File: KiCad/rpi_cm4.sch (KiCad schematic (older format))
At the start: 8 parts

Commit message: Update schematic
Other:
- note added: "check pull ups/downs on RPi power control pins"
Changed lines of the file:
@@
 $Descr A4 11693 8268
 encoding utf-8
-Sheet 3 5
+Sheet 2 5
 Title "RPi Compute Module 4 Section"
 Date "2020-12-03"
@@
 	1    0    0    -1
 $EndComp
+Text Notes 800  6250 0    50   ~ 0
+check pull ups/downs on RPi power control pins
 $EndSCHEMATC

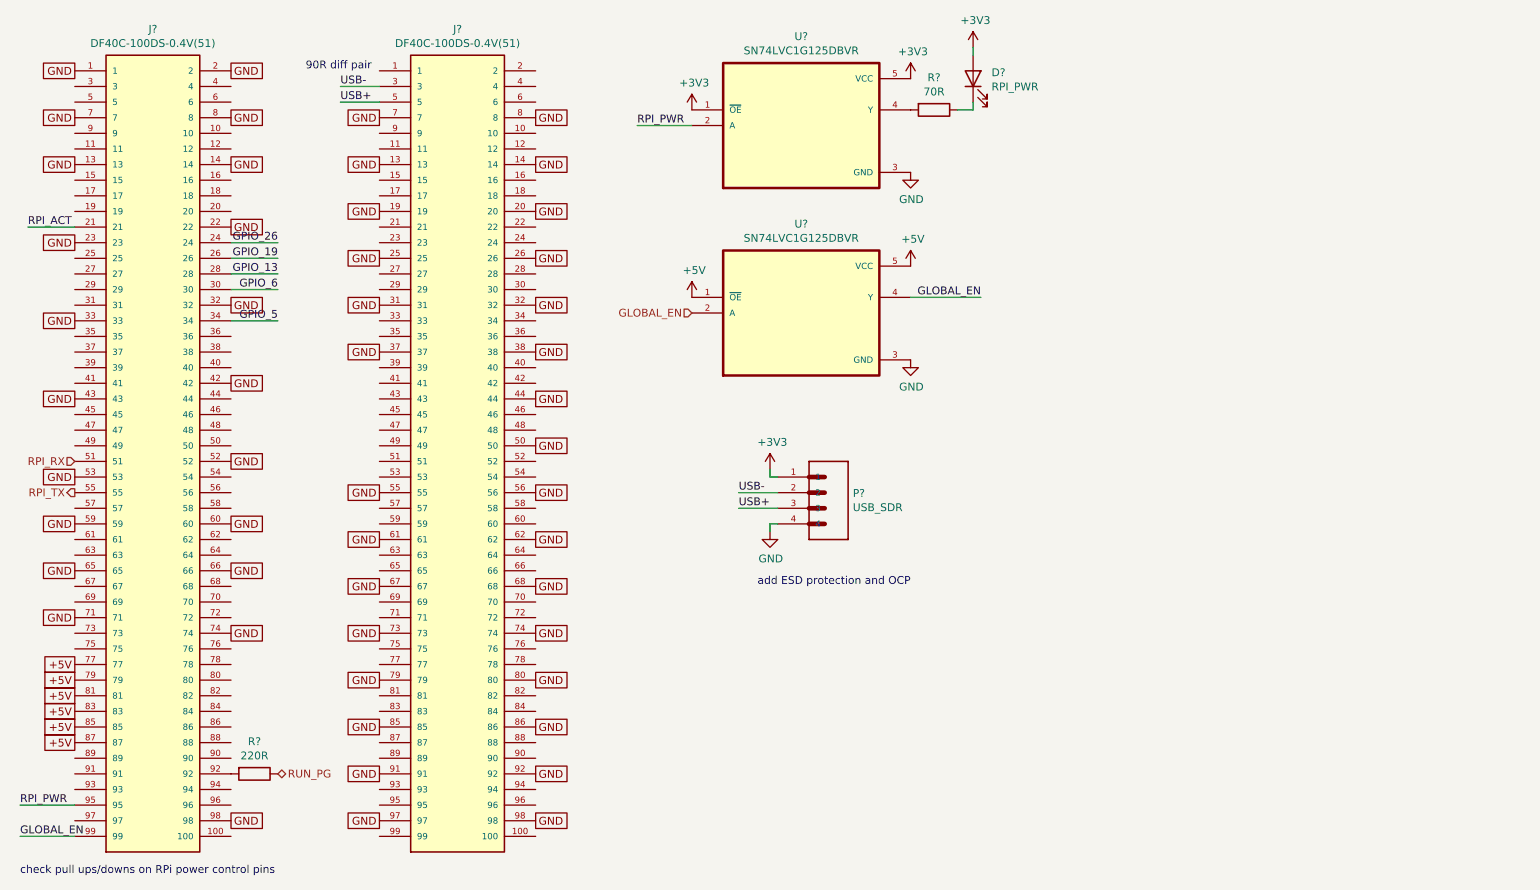
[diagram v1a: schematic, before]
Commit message: Finalized schematic and created S/F associations
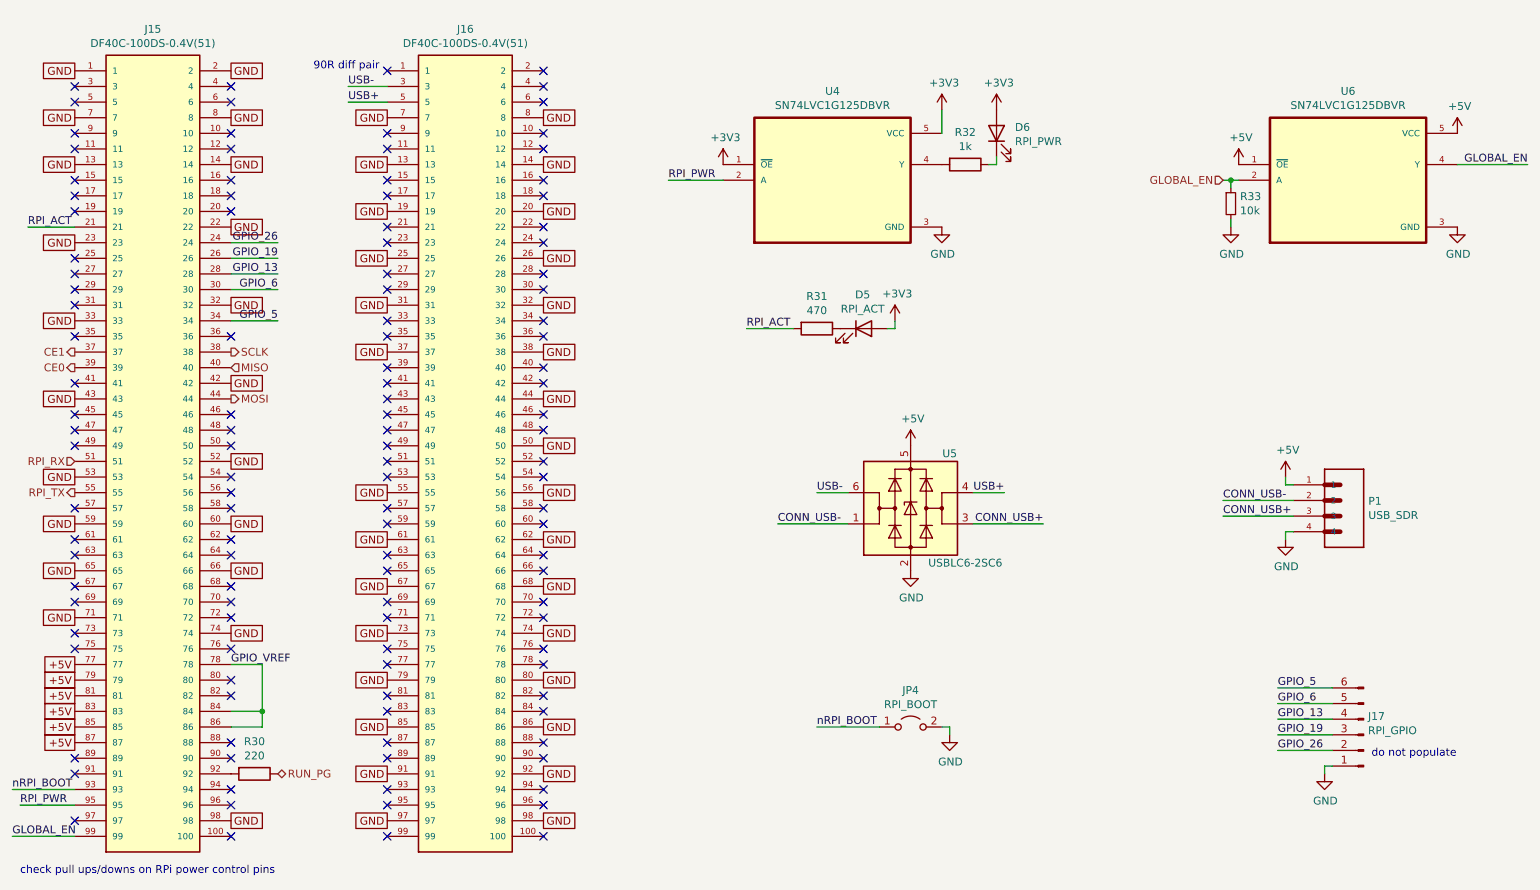
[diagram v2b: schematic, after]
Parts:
- added D5: RPI_ACT, LED_SMD:LED_0603_1608Metric_Pad1.05x0.95mm_HandSolder, symbol Device:LED
- added J17: RPI_GPIO, Connector_PinHeader_1.00mm:PinHeader_1x06_P1.00mm_Vertical, symbol Connector:Conn_01x06_Male
- added JP4: RPI_BOOT, TestPoint:TestPoint_2Pads_Pitch2.54mm_Drill0.8mm, symbol Jumper:Jumper_2_Open
- added R31: 470, Resistor_SMD:R_0603_1608Metric_Pad1.05x0.95mm_HandSolder, symbol Device:R
- added R33: 10k, Resistor_SMD:R_0603_1608Metric_Pad1.05x0.95mm_HandSolder, symbol Device:R_Small
- added U5: USBLC6-2SC6, Package_TO_SOT_SMD:SOT-23-6, symbol Power_Protection:USBLC6-2SC6
- D6: renamed from D?; footprint (none) -> LED_SMD:LED_0603_1608Metric_Pad1.05x0.95mm_HandSolder
- J15, J16: renamed from J?; footprint HRS_DF40C-100DS-0.4V(51) -> Libs:HRS_DF40C-100DS-0.4V(51)
- P1: renamed from P?; footprint TE_1734366-1 -> Libs:TE_1734366-1
- R30: renamed from R?; value 220R -> 220; footprint (none) -> Resistor_SMD:R_0603_1608Metric_Pad1.05x0.95mm_HandSolder
- R32: renamed from R?; value 70R -> 1k; footprint (none) -> Resistor_SMD:R_0603_1608Metric_Pad1.05x0.95mm_HandSolder
- U4, U6: renamed from U?; footprint SOT95P280X145-5N -> Libs:SOT95P280X145-5N
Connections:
- net +3V3: now also D5.2 (A); no longer P1.1
- net +5V: now also P1.1, U5.5 (VBUS)
- net GLOBAL_EN: now also R33.1
- net GND: now also J17.1 (Pin_1), JP4.2 (B), R33.2, U5.2 (GND)
- net GPIO_13: now also J17.4 (Pin_4)
- net GPIO_19: now also J17.3 (Pin_3)
- net GPIO_26: now also J17.2 (Pin_2)
- net GPIO_5: now also J17.6 (Pin_6)
- net GPIO_6: now also J17.5 (Pin_5)
- net RPI_ACT: now also R31.2
- net USB+: now also U5.4 (I/O2); no longer P1.3
- net USB-: now also U5.6 (I/O1); no longer P1.2
- net CE1: now reaches J15.37
- net SCLK: now reaches J15.38
- net CE0: now reaches J15.39
- net MISO: now reaches J15.40
- net MOSI: now reaches J15.44
- net GPIO_VREF: now reaches J15.78
- net GPIO_VREF: now also J15.84, J15.86
- net nRPI_BOOT: now reaches J15.93
- net nRPI_BOOT: now also JP4.1 (A)
- new net: D5.1 (K), R31.1
- new net CONN_USB+: P1.3, U5.3 (I/O2)
- new net CONN_USB-: P1.2, U5.1 (I/O1)
- no-connect marks 0 -> 121
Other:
- note added: "do not populate"
- note removed: "add ESD protection and OCP"
- moved on the sheet: D6, J16, P1, R32, U4, U6

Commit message: Semi-final flight computer version
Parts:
- removed U4, U6: SN74LVC1G125DBVR, Libs:SOT95P280X145-5N, symbol SN74LVC1G125DBVR:SN74LVC1G125DBVR
- added U4, U6: SN74LVC1G125DCKT, Libs:SOT65P210X110-5N, symbol SN74LVC1G125DCKT:SN74LVC1G125DCKT
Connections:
- net +3V3: now also U4.1 (~OE), U4.5 (VCC)
- net +5V: now also U6.1 (~OE), U6.5 (VCC)
- net GLOBAL_EN: now also U6.2 (A); no longer J15.99
- net GND: now also U4.3 (GND), U6.3 (GND)
- net RPI_PWR: now also U4.2 (A)
- net at R32.2: now also U4.4 (Y)
- new net RPI_ENABLE: J15.99, U6.4 (Y)
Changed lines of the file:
@@
 	750  6000 1150 6000
 Text Label 750  6000 0    50   ~ 0
-GLOBAL_EN
+RPI_ENABLE
 $Comp
 L Device:R R30
@@
 GPIO_5
 $Comp
-L SN74LVC1G125DBVR:SN74LVC1G125DBVR U4
-U 1 1 5FCBE30F
-P 6000 1800
-F 0 "U4" H 6000 2370 50  0000 C CNN
-F 1 "SN74LVC1G125DBVR" H 6000 2279 50  0000 C CNN
-F 2 "Libs:SOT95P280X145-5N" H 6000 1800 50  0001 L BNN
-F 3 "" H 6000 1800 50  0001 L BNN
-	1    6000 1800
-	1    0    0    -1
-$EndComp
-$Comp
-L SN74LVC1G125DBVR:SN74LVC1G125DBVR U6
-U 1 1 5FCBF4AC
-P 9300 1800
-F 0 "U6" H 9300 2370 50  0000 C CNN
-F 1 "SN74LVC1G125DBVR" H 9300 2279 50  0000 C CNN
-F 2 "Libs:SOT95P280X145-5N" H 9300 1800 50  0001 L BNN
-F 3 "" H 9300 1800 50  0001 L BNN
-	1    9300 1800
-	1    0    0    -1
-$EndComp
-$Comp
 L power:+3V3 #PWR0147
 U 1 1 5FCC0A7C
@@
 $EndComp
 Text Label 10450 1700 2    50   ~ 0
-GLOBAL_EN
+RPI_ENABLE
 Wire Wire Line
 	10450 1700 10000 1700
@@
 Wire Wire Line
 	8550 2100 8550 2050
+$Comp
+L SN74LVC1G125DCKT:SN74LVC1G125DCKT U4
+U 1 1 5FCF5FD7
+P 6000 1800
+F 0 "U4" H 6000 2370 50  0000 C CNN
+F 1 "SN74LVC1G125DCKT" H 6000 2279 50  0000 C CNN
+F 2 "Libs:SOT65P210X110-5N" H 6000 1800 50  0001 L BNN
+F 3 "" H 6000 1800 50  0001 L BNN
+	1    6000 1800
+	1    0    0    -1
+$EndComp
+$Comp
+L SN74LVC1G125DCKT:SN74LVC1G125DCKT U6
+U 1 1 5FCF7288
+P 9300 1800
+F 0 "U6" H 9300 2370 50  0000 C CNN
+F 1 "SN74LVC1G125DCKT" H 9300 2279 50  0000 C CNN
+F 2 "Libs:SOT65P210X110-5N" H 9300 1800 50  0001 L BNN
+F 3 "" H 9300 1800 50  0001 L BNN
+	1    9300 1800
+	1    0    0    -1
+$EndComp
 $EndSCHEMATC
